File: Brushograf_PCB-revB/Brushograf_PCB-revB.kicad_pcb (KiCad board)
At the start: 2 copper layers, 198 x 73 mm, 77 parts, among them J1 Conn_01x05_Socket, J12 USB-C PD in, J13 Pendant, J2 Conn_01x05_Socket, J3 Conn_01x05_Socket, J6 Conn_01x07_Socket, J7 Conn_01x03_Pin, J8 SD_CARD_MICRO_AMPHENOL_114008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, SW1 ESP POWER, U1 ULN2003A, U2 ULN2003A, U3 ULN2003A, U4 ESP32-DevKitC, U6 CH224K, U7 TPS54202, U8 TPS54202

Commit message: Update SW2 to switch, move SW1 for hole clearance, relocate SD card holder to edge
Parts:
- removed J7: Conn_01x03_Pin, Connector_Molex:Molex_KK-254_AE-6410-03A_1x03_P2.54mm_Vertical
- added SW2: SW_Lever_1P2T_NKK_GW12LxH, SW_Lever_1P2T_NKK_GW12LxH, F.Cu at (51.5, 99.3)
- moved J8 24.4 mm to (90.0, 71.0), turned to 0 degrees
- moved F1 2.50 mm to (66.5, 66.0)
- moved SW1 2.50 mm to (60.5, 66.0)

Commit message: Fix component packing and shrink board outline correctly
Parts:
- removed J6: Conn_01x07_Socket, 007_dusjagr:Molex_KK-254_AE-6410-07A_1x07_P2.54mm_Vertical
- removed R13, R14: 0, 007_dusjagr:R_1206_noGND
- removed Ref**: Val**, 009_Brushograph:CoconutLogo2
- removed Ref**: Val**, 009_Brushograph:brushograf_edgeCut
- moved U2 186.8 mm to (41.3, 92.4), turned to 0 degrees
- moved D8 186.4 mm to (33.1, 153.3), turned to 0 degrees
- moved D6 184.8 mm to (41.3, 146.4), turned to 0 degrees
- moved R29 182.4 mm to (37.1, 160.0)
- moved D5 172.4 mm to (57.8, 146.4), turned to 0 degrees
- moved R7 171.9 mm to (46.7, 166.2), turned to 0 degrees
- moved C17 158.7 mm to (43.6, 124.3)
- moved R8 157.4 mm to (60.9, 166.2), turned to 0 degrees
- moved R30 155.7 mm to (42.5, 160.0)
- moved D19 154.5 mm to (35.3, 132.2)
- moved R5 154.0 mm to (67.9, 166.2), turned to 0 degrees
- moved J2 151.3 mm to (90.0, 50.0), turned to 90 degrees
- moved D7 150.9 mm to (70.7, 139.3), turned to 0 degrees
- moved R28 145.5 mm to (70.0, 153.1)
- moved R6 145.4 mm to (73.5, 159.7), turned to 0 degrees
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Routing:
- net 5V: track 249.9 -> 0.00 mm, vias 1 -> 0
- net IN4_U2: track 198.7 -> 0.00 mm
- net IN3_U2: track 198.4 -> 0.00 mm
- net IN2_U2: track 189.4 -> 0.00 mm
- net IN1_U2: track 184.6 -> 0.00 mm
- net IN1_U1: track 141.7 -> 0.00 mm, vias 1 -> 0
- net IN2_U1: track 135.9 -> 0.00 mm
- net IN3_U1: track 125.1 -> 0.00 mm
- net IN4_U1: track 119.7 -> 0.00 mm
- net MISO: track 81.8 -> 0.00 mm, vias 2 -> 0
- net IN1_U3: track 81.4 -> 0.00 mm
- net CS: track 81.0 -> 0.00 mm, vias 1 -> 0
- net IN2_U3: track 75.4 -> 0.00 mm
- net SCK: track 68.7 -> 0.00 mm, vias 3 -> 0
- net IN3_U3: track 68.0 -> 0.00 mm
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- removed copper zone on B.Cu, net GND
- removed copper zone on F.Cu, net GND
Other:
- board size 198 x 73 mm -> 77 x 160.1 mm

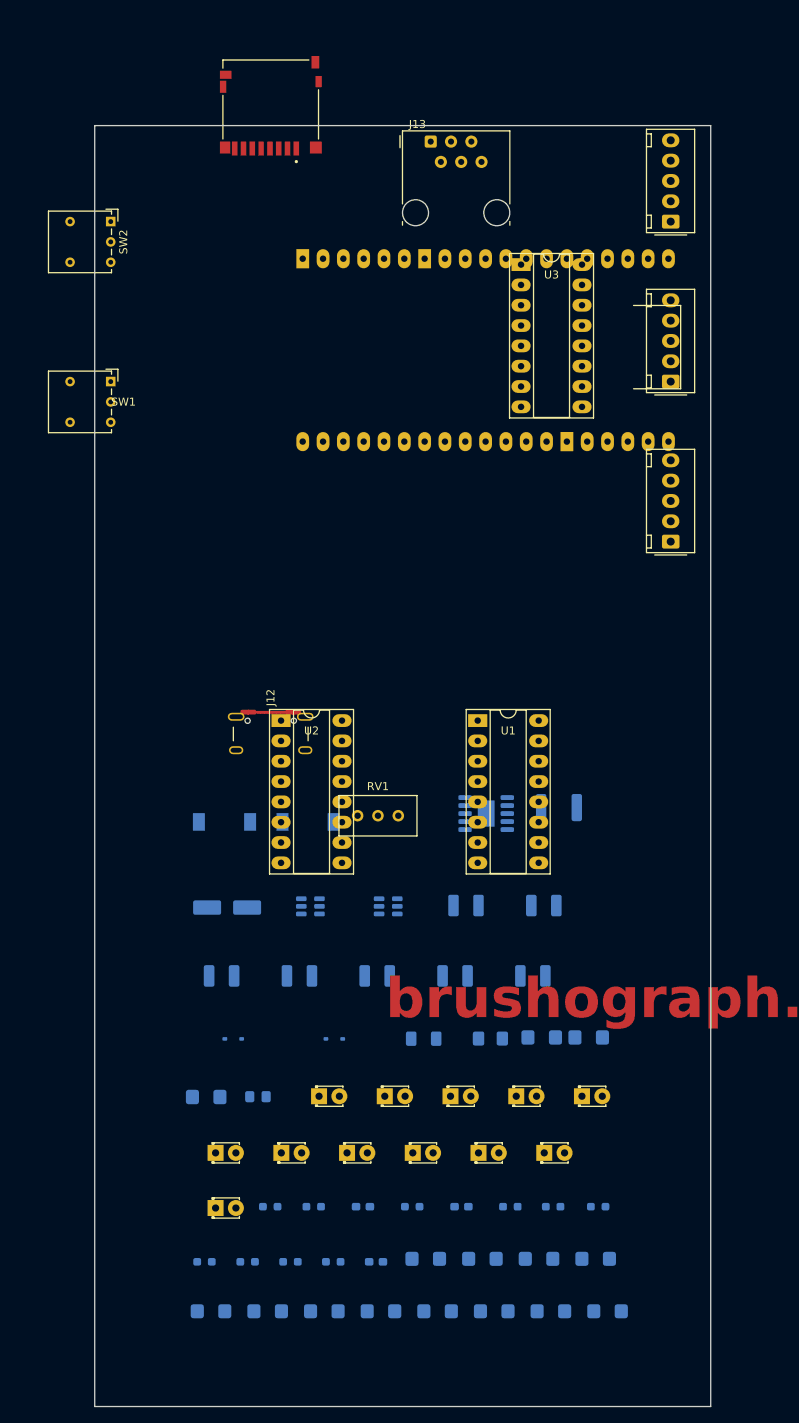
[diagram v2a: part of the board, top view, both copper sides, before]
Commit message: Repack components with ESP32 clearance, edge alignment for SD, and LED grouping
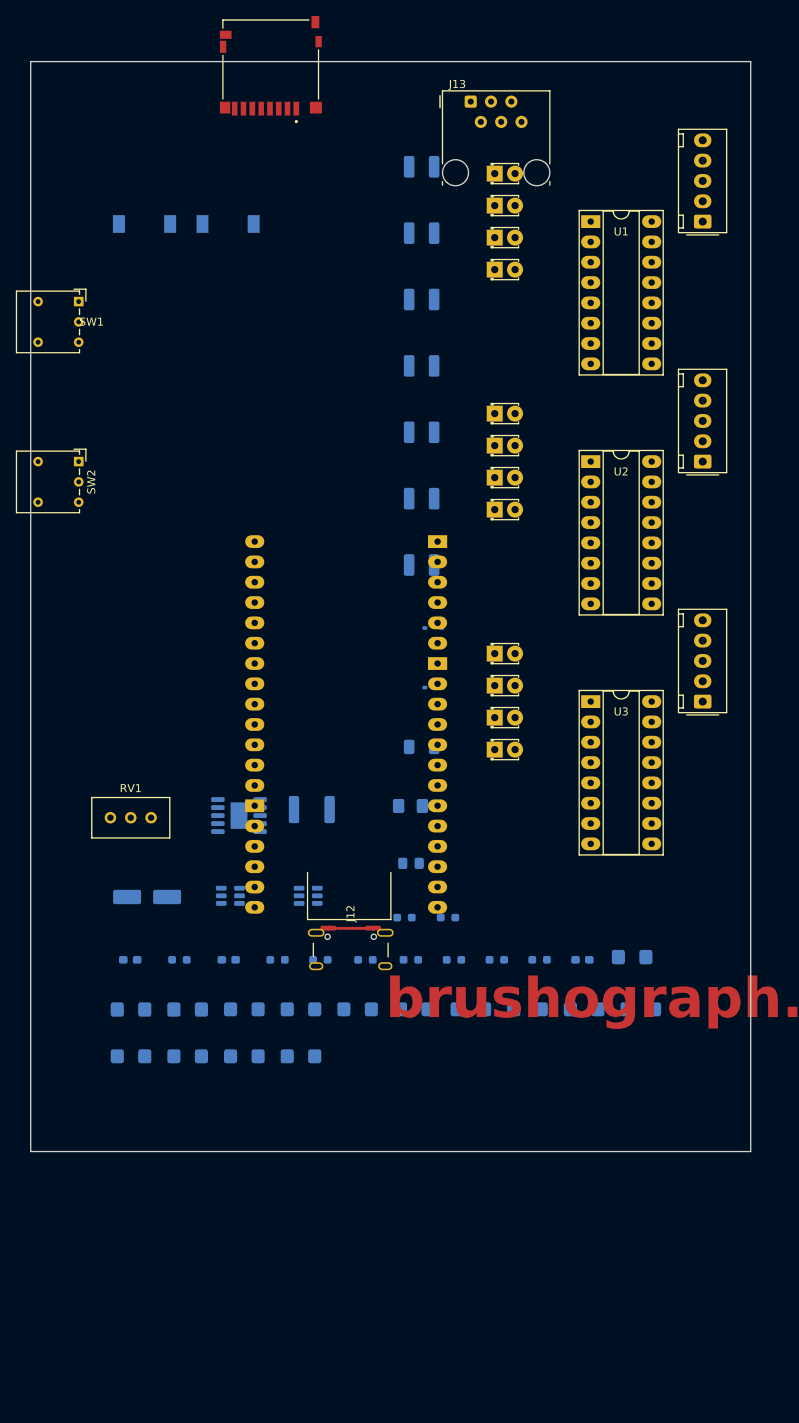
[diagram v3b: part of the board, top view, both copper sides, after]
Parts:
- moved D1 122.6 mm to (68.0, 24.0)
- moved D3 115.9 mm to (68.0, 32.0)
- moved D2 113.5 mm to (68.0, 28.0)
- moved D4 110.4 mm to (68.0, 36.0)
- moved D8 94.0 mm to (68.0, 66.0)
- moved D5 93.0 mm to (68.0, 54.0)
- moved C11 92.5 mm to (58.9, 23.1)
- moved D6 92.3 mm to (68.0, 58.0)
- moved C8 88.2 mm to (58.9, 39.7)
- moved C10 85.4 mm to (58.9, 31.4)
- moved C17 77.8 mm to (58.9, 48.0)
- moved D7 77.4 mm to (68.0, 62.0)
- moved L1 75.4 mm to (24.2, 30.3)
- moved L2 75.4 mm to (34.7, 30.3)
- moved C15 68.2 mm to (58.9, 56.3)
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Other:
- board size 77 x 160.1 mm -> 90 x 136.2 mm

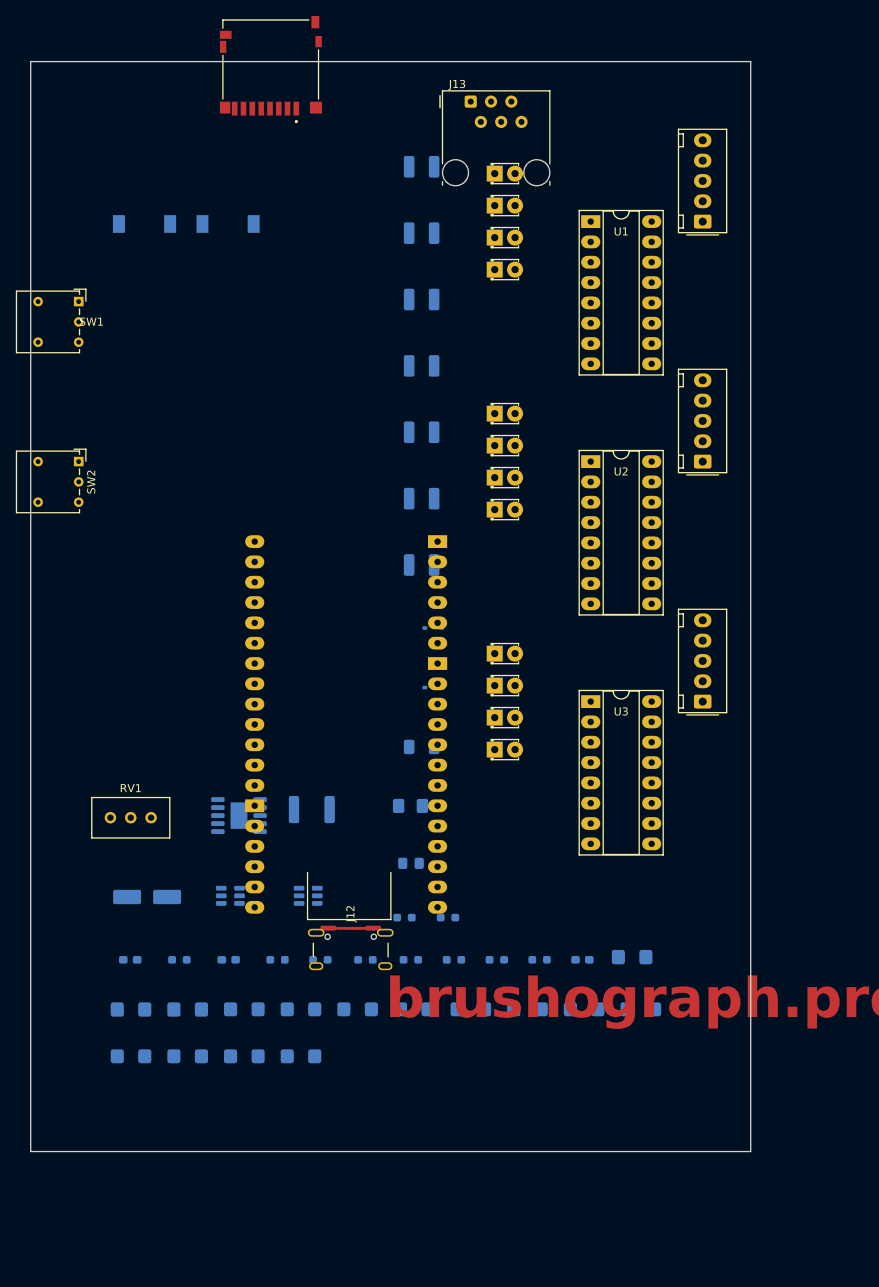
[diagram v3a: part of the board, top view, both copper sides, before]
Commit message: Align Top/Left edge components per user request
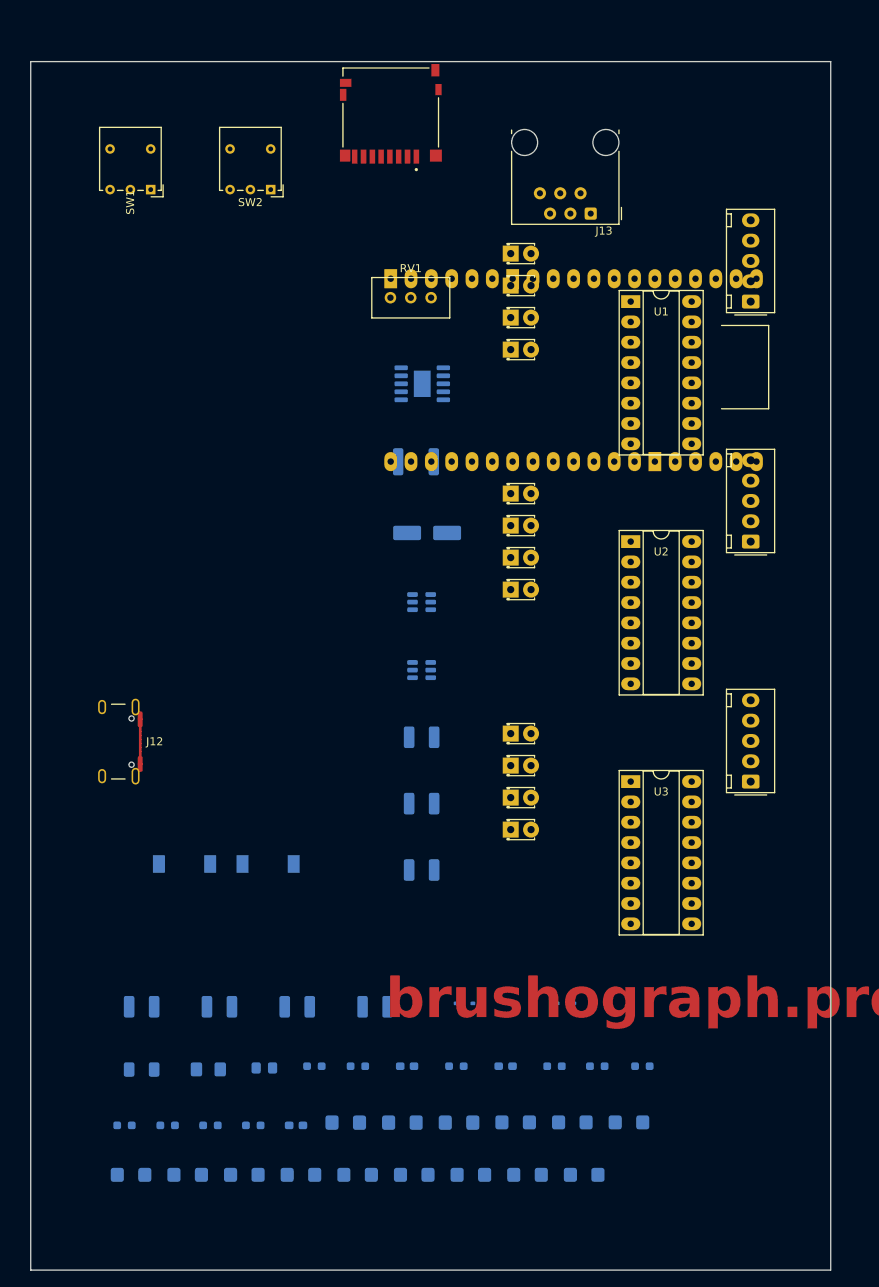
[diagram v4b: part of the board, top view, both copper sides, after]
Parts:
- moved C17 87.4 mm to (23.9, 128.1)
- moved L1 80.2 mm to (29.2, 110.3)
- moved L2 80.2 mm to (39.7, 110.3)
- moved C15 76.1 mm to (33.6, 128.1)
- moved RV1 73.8 mm to (60.0, 39.5)
- moved C10 71.3 mm to (58.9, 102.8)
- moved C11 71.3 mm to (58.9, 94.5)
- moved C8 71.3 mm to (58.9, 111.1)
- moved C14 65.4 mm to (43.3, 128.1)
- moved U6 58.6 mm to (58.9, 50.3)
- moved D14 57.4 mm to (59.5, 68.9)
- moved C13 55.5 mm to (53.0, 128.1)
- moved C7 53.4 mm to (23.9, 136.0)
- moved D19 47.1 mm to (64.2, 127.7)
- moved F1 45.4 mm to (58.2, 60.0)
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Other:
- board size 90 x 136.2 mm -> 100 x 151.1 mm

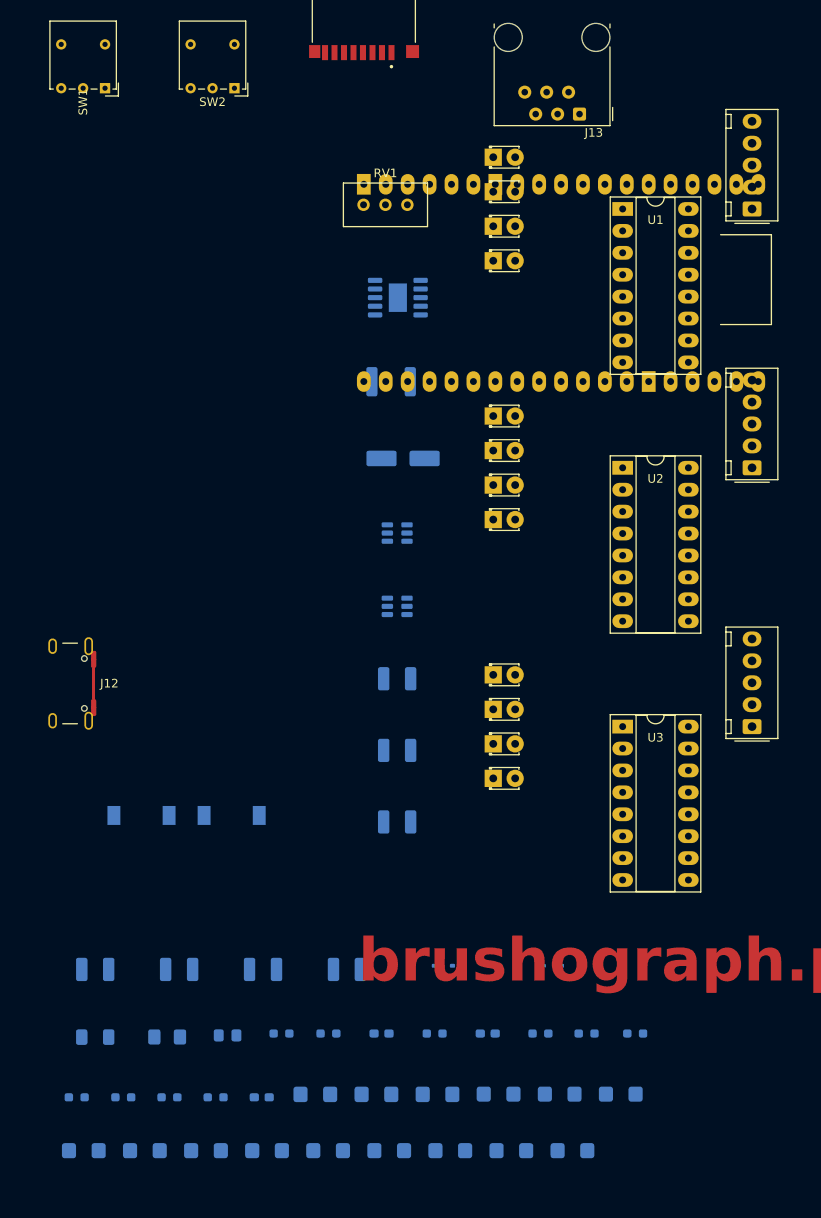
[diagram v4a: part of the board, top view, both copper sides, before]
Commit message: Auto-route traces using FreeRouting
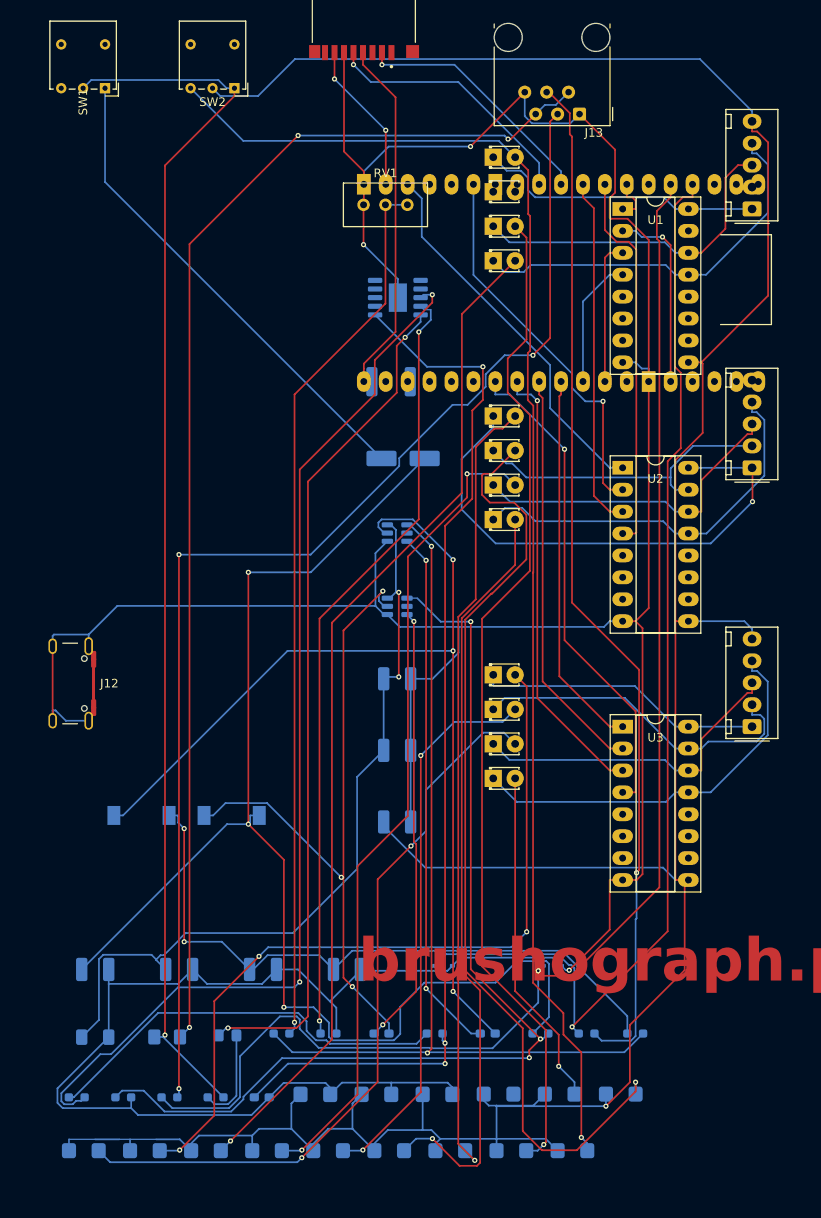
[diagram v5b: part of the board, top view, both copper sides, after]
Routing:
- net GND: track 0.00 -> 436.8 mm, vias 0 -> 3
- net 5V: track 0.00 -> 354.8 mm, vias 0 -> 1
- net PEND_TX: track 0.00 -> 161.0 mm, vias 0 -> 1
- net Net-(D1-A): track 0.00 -> 159.8 mm, vias 0 -> 1
- net 5V_LOGIC: track 0.00 -> 154.4 mm, vias 0 -> 3
- net PEND_TX_CON: track 0.00 -> 144.1 mm, vias 0 -> 3
- net PEND_5V: track 0.00 -> 143.9 mm, vias 0 -> 3
- net 5V_SYS: track 0.00 -> 142.6 mm, vias 0 -> 1
- net PEND_RX: track 0.00 -> 130.1 mm, vias 0 -> 1
- net Net-(U6-VBUS): track 0.00 -> 124.6 mm, vias 0 -> 2
- net Net-(U6-VDD): track 0.00 -> 122.5 mm, vias 0 -> 3
- net PEND_RX_CON: track 0.00 -> 119.5 mm, vias 0 -> 1
- net Net-(D4-A): track 0.00 -> 117.3 mm, vias 0 -> 1
- net Net-(U7-SW): track 0.00 -> 116.8 mm, vias 0 -> 3
- net Net-(D3-A): track 0.00 -> 116.8 mm, vias 0 -> 1
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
